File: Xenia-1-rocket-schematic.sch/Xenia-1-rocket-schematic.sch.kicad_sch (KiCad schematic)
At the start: 33 parts, among them M1 Stepper_Motor_bipolar, U3 A1115, U6 BME280, U7 Black_Box

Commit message: Schematic updated
Added a several new labels on the wiring diagram and made a section for the recovery altimeters, also made the e-matches necessary to light the black powder. Added recurring labels to wires on the right side and marked many ports with no X's to mean that they will not be connected to anything during wiring.
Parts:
- added U? (x8): E-Match, symbol Rocketry_project:E-Match
- added U? (x2): Raven4, symbol Rocketry_project:Raven4
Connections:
- net SDA is gone; now on net I2C Data: A?.3 (GPIO2/SDA), U?. (VDD), U?. (V_in), U?.~ (V_in), U?.~ (V_in)
- net +9V: now also U?.~ (V_in), U?.~ (V_in)
- net GND: now also A?.7 (GPIO4/GPCKL0), U?. (PCM_DOUT), U?. (Input), U?. (Input), U?. (Input), U?. (Input), U?. (Input), U?. (Input), U?. (Input), U?. (Input), U?.~ (V_in), U?.~ (V_in)
- net I2C Data: now reaches U?.~ (V_in)
- net APO: now reaches U?.~ (V_in)
- net APO: now also U?.~ (V_in), U?. (Input), U?. (Input), U?. (Input), U?. (Input), U?. (Input), U?. (Input), U?. (Input), U?. (Input)
- removed net GPIO4/Sleep: A?.7 (GPIO4/GPCKL0), U?. (PCM_DOUT), U?. (VMOT)
- removed net SCL: A?.5 (GPIO3/SCL), U?. (VDD), U?. (V_in), U?.~ (V_in), U?.~ (V_in)
- new net E-Match: U?.~ (V_in), U?.~ (V_in)
- new net I2C Clock: A?.5 (GPIO3/SCL), U?. (VDD), U?. (V_in), U?.~ (V_in), U?.~ (V_in)
- no-connect marks 30 -> 74
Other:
- note added: "Recovery Altimeters"

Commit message: Updated Schematic
Added a second sheet, and made a new version of the schematic that is a lot more organized
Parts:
- removed U? (x4): E-Match, symbol Rocketry_project:E-Match
- removed U? (x2): Transmitter, symbol Rocketry_project:Transmitter
- removed U?: Buzzer, symbol Rocketry_project:Buzzer
- added A?: rPi0w2, ADA3708_RPI-ZERO, symbol ADA3708:rPi0w2
- added BT? (x2): Battery_Cell, symbol Device:Battery_Cell
- added C?: CAP, symbol pspice:CAP
- added M?: Stepper_Motor_bipolar, symbol Motor:Stepper_Motor_bipolar
- added RV?: R_Potentiometer, symbol Device:R_Potentiometer
- added U1, U11, U12, U2, U? (x4): E-Match, symbol Rocketry_project:E-Match
- added U10, U31, U?: Transmitter, symbol Rocketry_project:Transmitter
- added U9, U?: Buzzer, symbol Rocketry_project:Buzzer
- added U?: Strain Gauge PCB, symbol Rocketry_project:Strain Gauge PCB
- added U? (x2): Raven4, symbol Rocketry_project:Raven4
- added U?: Camera, symbol Rocketry_project:Camera
- added U?: LSM9DS1, symbol Rocketry_project:LSM9DS1
- added U?: ADXL375, symbol Rocketry_project:ADXL375
- added U?: A1115, symbol Rocketry_project:A1115
- added U?: DRV8825, symbol Rocketry_project:DRV8825
- added U?: Black_Box, symbol Rocketry_project:Black_Box
- added U?: BME280, symbol Rocketry_project:BME280
- gave numbers to parts that had none: 31
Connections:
- net +3V8: now also U10. (TTL-DOUT)
- net 3V3: now also A?.1 (3V3[1]), U?. (V_in), U?.~ (V_in), U?.~ (V_in)
- net 5V: now also A?.2 (5V[1]), RV?.1, U?. (PCM_DOUT), U?. (VDD), U?. (VMOT)
- net APO: now also U1. (Input), U11. (Input), U2. (Input), U?. (Input), U?. (Input), U?. (Input), U?. (Input), U?.~ (V_in), U?.~ (V_in)
- net DIR: now also A?.26 (~{CE1/}GPIO7), U?. (PWR), U?. (VMOT)
- net Enable: now also A?.12 (GPIO18), U?. (VMOT)
- net GND: now also A?.9 (GND[1]), RV?.3, U1. (Input), U10. (TTL-DOUT), U11. (Input), U12. (Input), U2. (Input), U31. (TTL-DOUT), U9. (PWR), U?. (Input), U?. (Input), U?. (Input), U?. (Input), U?. (PCM_DOUT), U?. (PWR), U?. (TTL-DOUT), U?. (VDD), U?. (VMOT), U?. (V_in), U?.~ (V_in), U?.~ (V_in)
- net GPIO14: now also U10. (TTL-DOUT)
- net GPIO15: now also U10. (TTL-DOUT)
- net GPIO7: now also U9. (PWR)
- net I2C Clock: now also A?.5 (GPIO3/SCL), U?. (VDD), U?. (V_in), U?.~ (V_in), U?.~ (V_in)
- net I2C Data: now also A?.3 (GPIO2/SDA), U?. (VDD), U?. (V_in), U?.~ (V_in), U?.~ (V_in)
- net Step: now also A?.24 (~{CE0}/GPIO8), U?. (VMOT)
- net TTL-DIN: now also A?.8 (TXD0/GPIO14), U?. (TTL-DOUT)
- net TTL-DOUT: now also A?.10 (RXD0/GPIO15), U?. (TTL-DOUT)
- net at A2.10 (RXD0/GPIO15): now also U31. (TTL-DOUT)
- net at A2.8 (TXD0/GPIO14): now also U31. (TTL-DOUT)
- new net: A?. (Camera), U?.~ (Port)
- new net: A?.38 (GPIO20), U?. (PCM_DOUT)
- new net: A?.40 (GPIO21), U?. (PCM_DOUT)
- new net: A?.7 (GPIO4/GPCKL0), U?. (VMOT)
- new net: RV?.2, U?. (VDD)
- new net: BT?.1 (+), U?.~ (V_in) (x2)
- new net: BT?.2 (-), U?.~ (V_in) (x2)
- new net: M?.1, U?. (VMOT)
- new net: M?.2 (-), U?. (VMOT)
- new net: M?.3, U?. (VMOT)
- new net: M?.4, U?. (VMOT)
- new net: C?.1, U?. (VMOT)
- new net: C?.2, U?. (VMOT)
- no-connect marks 74 -> 73
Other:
- added sheet Sample wiring (untitled.kicad_sch)

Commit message: Updated Schematic
Made a couple adjustments to the schematic with the size of things and put a couple labels up
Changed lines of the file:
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@@
     (pin "1")
   )
-  (sheet (at 594.36 73.66) (size 748.03 304.8) (fields_autoplaced)
+  (sheet (at 594.36 73.66) (size 643.89 304.8) (fields_autoplaced)
     (stroke (width 0.1524) (type solid) (color 0 0 0 0))
     (fill (color 0 0 0 0.0000))

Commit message: Updated schematic
Added some labels to the second version of the wired schematic about what sides of the avionics bay things went to.
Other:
- note added: "Bottom of Avionics Bay"
- note added: "Top of Avionics Bay"
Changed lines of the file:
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@@
     (effects (font (size 3 3)) (justify left bottom))
+  )
+  (text "Side A" (at 1112.52 86.36 0)
+    (effects (font (size 2 2)) (justify left bottom))
   )
   (text "Side D" (at 524.51 209.55 0)
     (effects (font (size 3 3)) (justify left bottom))
+  )
+  (text "Top of Avionics Bay" (at 1167.13 83.82 0)
+    (effects (font (size 2 2)) (justify left bottom))
+  )
+  (text "Side B" (at 1112.52 144.78 0)
+    (effects (font (size 2 2)) (justify left bottom))
   )
   (text "Side A" (at 543.56 294.64 0)
@@
   (text "Inputs" (at 161.29 58.42 0)
     (effects (font (size 4 4)) (justify left bottom))
+  )
+  (text "Side C" (at 1109.98 231.14 0)
+    (effects (font (size 2 2)) (justify left bottom))
   )
   (text "Recovery Altimeters" (at 54.61 242.57 0)
@@
     (effects (font (size 1.27 1.27)) (justify left bottom))
   )
+  (text "Side D" (at 1111.25 293.37 0)
+    (effects (font (size 2 2)) (justify left bottom))
+  )
   (text "Analog to Digital Convertor" (at 240.03 143.51 0)
     (effects (font (size 1.27 1.27)) (justify left bottom))
   )
+  (text "Bottom of Avionics Bay" (at 645.16 102.87 0)
+    (effects (font (size 2 2)) (justify left bottom))
+  )
   (label "PCM_DOUT" (at 77.47 180.34 0)

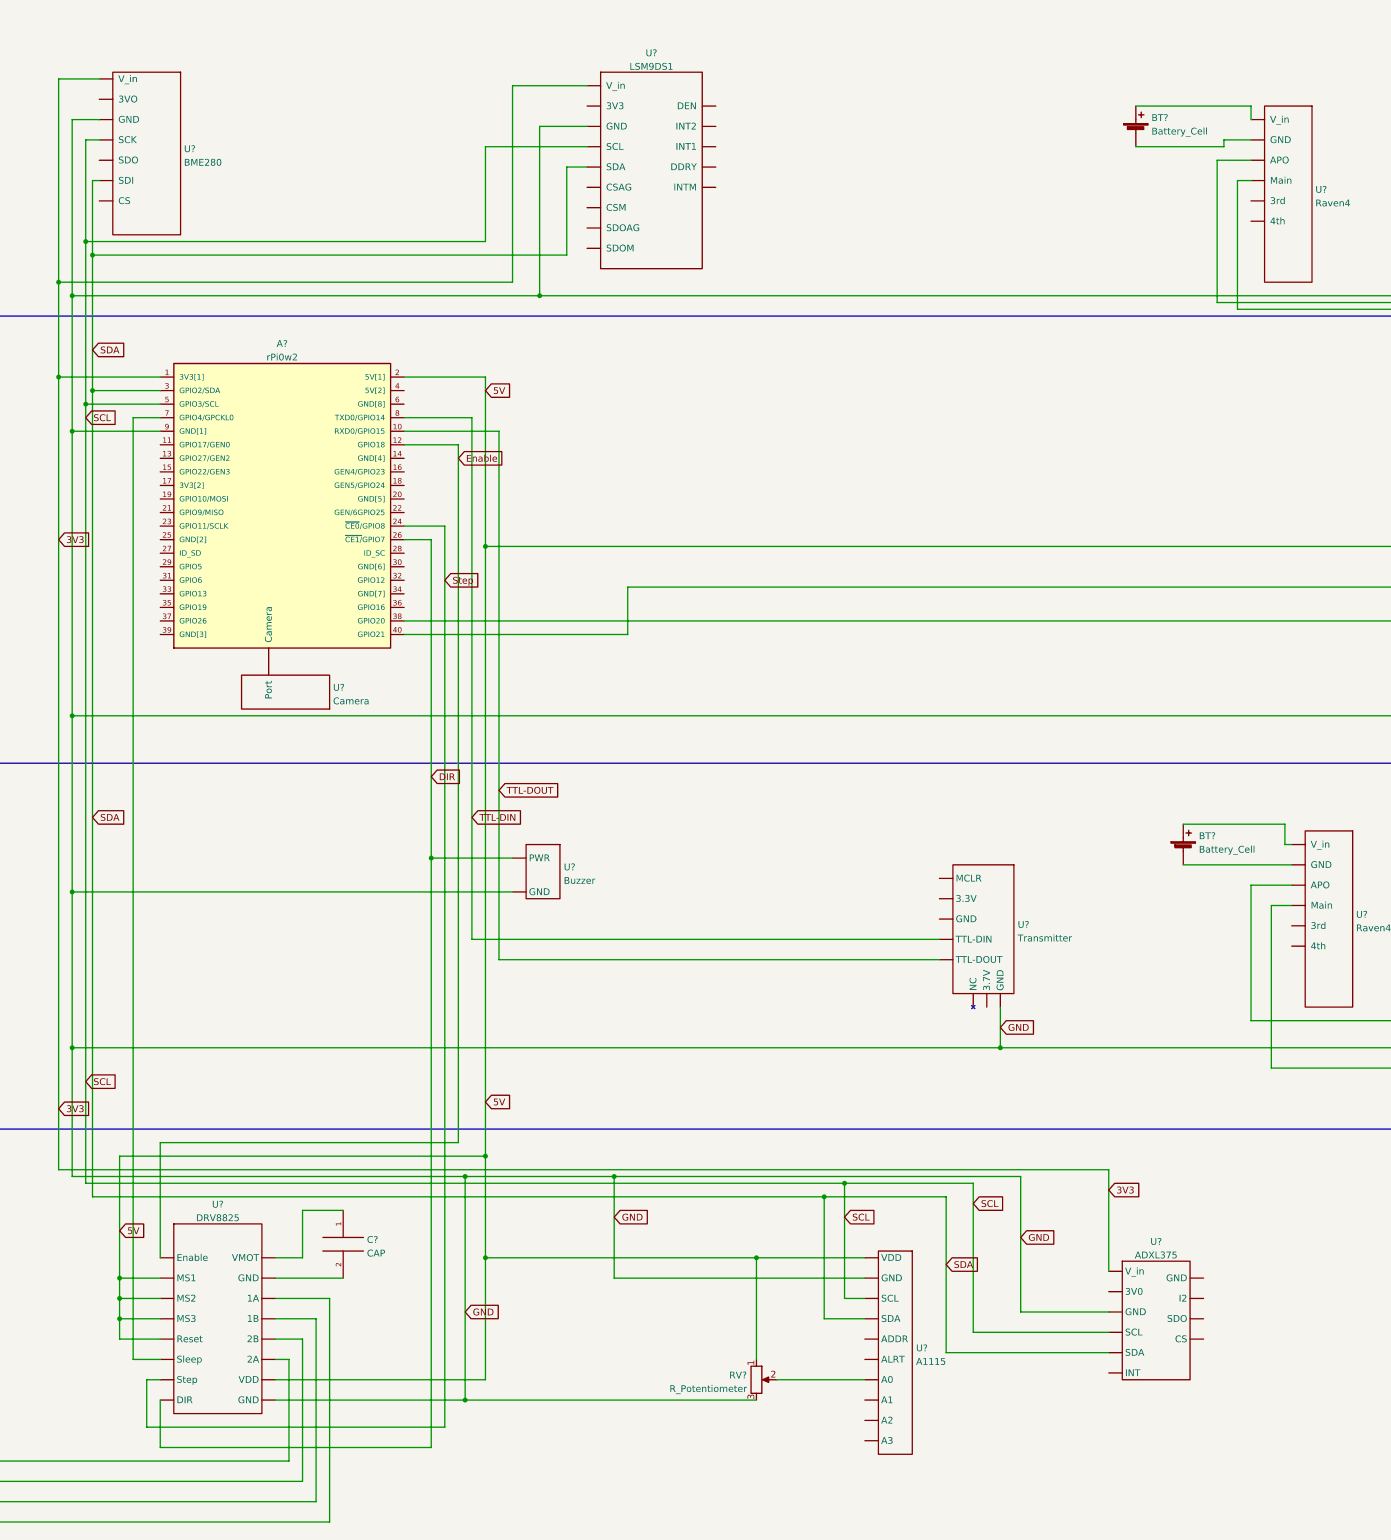
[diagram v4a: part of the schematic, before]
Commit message: Updated schematic
Marked many ports with no connect
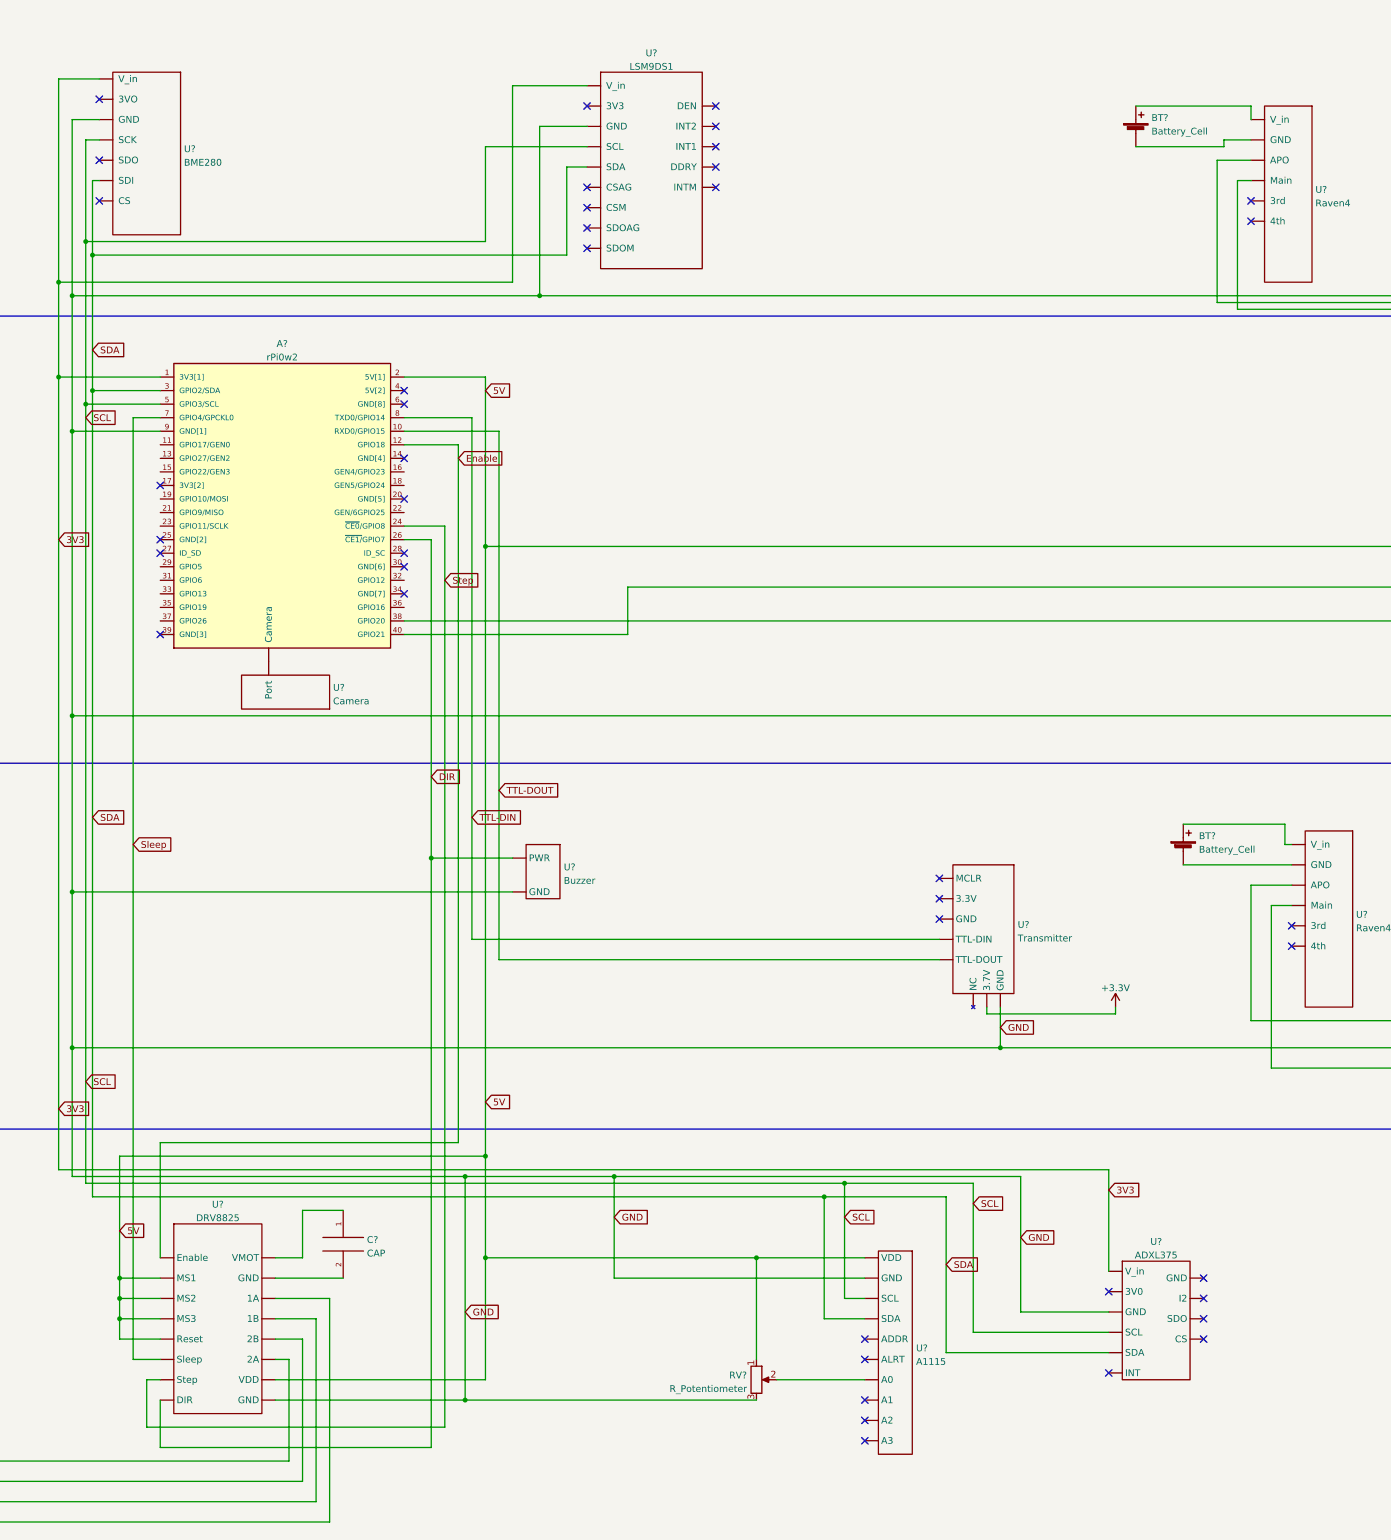
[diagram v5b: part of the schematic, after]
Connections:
- net +3V3: now also U?. (TTL-DOUT)
- net Sleep: now also A?.7 (GPIO4/GPCKL0), U?. (VMOT)
- no-connect marks 73 -> 115
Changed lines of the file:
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@@
   (no_connect (at 201.93 170.18))
   (no_connect (at 201.93 173.99))
+  (no_connect (at 932.18 111.76))
+  (no_connect (at 932.18 107.95))
+  (no_connect (at 932.18 104.14))
+  (no_connect (at 932.18 100.33))
+  (no_connect (at 932.18 96.52))
+  (no_connect (at 908.05 96.52))
+  (no_connect (at 908.05 111.76))
+  (no_connect (at 908.05 115.57))
+  (no_connect (at 908.05 119.38))
+  (no_connect (at 908.05 123.19))
+  (no_connect (at 816.61 114.3))
+  (no_connect (at 816.61 106.68))
+  (no_connect (at 816.61 95.25))
   (no_connect (at 146.05 158.75))
   (no_connect (at 146.05 143.51))
@@
   (no_connect (at 502.92 157.48))
   (no_connect (at 502.92 161.29))
+  (no_connect (at 873.76 187.96))
   (no_connect (at 100.33 62.23))
   (no_connect (at 100.33 58.42))
@@
   (no_connect (at 495.3 208.28))
   (no_connect (at 495.3 212.09))
+  (no_connect (at 873.76 149.86))
+  (no_connect (at 873.76 152.4))
+  (no_connect (at 873.76 162.56))
+  (no_connect (at 828.04 180.34))
+  (no_connect (at 828.04 177.8))
+  (no_connect (at 828.04 167.64))
+  (no_connect (at 873.76 170.18))
+  (no_connect (at 828.04 195.58))
+  (no_connect (at 873.76 182.88))
+  (no_connect (at 873.76 180.34))
   (no_connect (at 227.33 146.05))
   (no_connect (at 227.33 149.86))
@@
   (no_connect (at 227.33 196.85))
   (no_connect (at 227.33 177.8))
+  (no_connect (at 1032.51 114.3))
+  (no_connect (at 1032.51 118.11))
+  (no_connect (at 1040.13 250.19))
+  (no_connect (at 1040.13 254))
+  (no_connect (at 960.12 331.47))
+  (no_connect (at 960.12 339.09))
+  (no_connect (at 960.12 342.9))
+  (no_connect (at 960.12 327.66))
+  (no_connect (at 974.09 248.92))
+  (no_connect (at 974.09 245.11))
+  (no_connect (at 974.09 241.3))
+  (no_connect (at 960.12 346.71))
+  (no_connect (at 1005.84 334.01))
+  (no_connect (at 1005.84 318.77))
+  (no_connect (at 1023.62 316.23))
+  (no_connect (at 1023.62 320.04))
+  (no_connect (at 1023.62 323.85))
+  (no_connect (at 1023.62 327.66))
   (no_connect (at 77.47 165.1))
   (no_connect (at 77.47 167.64))
@@
     (stroke (width 0) (type default) (color 0 0 0 0))
   )
+  (wire (pts (xy 982.98 266.7) (xy 1007.11 266.7))
+    (stroke (width 0) (type default) (color 0 0 0 0))
+  )
   (wire (pts (xy 1158.24 140.97) (xy 1158.24 134.62))
     (stroke (width 0) (type default) (color 0 0 0 0))
@@
     (stroke (width 0) (type default) (color 0 0 0 0))
   )
+  (wire (pts (xy 982.98 265.43) (xy 982.98 266.7))
+    (stroke (width 0) (type default) (color 0 0 0 0))
+  )
   (wire (pts (xy 655.32 182.88) (xy 655.32 354.33))
     (stroke (width 0) (type default) (color 0 0 0 0))
@@
     (stroke (width 0) (type default) (color 0 0 0 0))
   )
+  (wire (pts (xy 1007.11 266.7) (xy 1007.11 265.43))
+    (stroke (width 0) (type default) (color 0 0 0 0))
+  )
   (wire (pts (xy 317.5 201.93) (xy 477.52 201.93))
     (stroke (width 0) (type default) (color 0 0 0 0))
@@
     )
   )
+  (global_label "Sleep" (shape input) (at 822.96 234.95 0) (fields_autoplaced)
+    (effects (font (size 1.27 1.27)) (justify left))
+    (property "Intersheet References" "${INTERSHEET_REFS}" (id 0) (at 830.4852 234.8706 0)
+      (effects (font (size 1.27 1.27)) (justify left) hide)
+    )
+  )
   (global_label "Main" (shape input) (at 513.08 62.23 0) (fields_autoplaced)
     (effects (font (size 1.27 1.27)) (justify left))
@@
     (pin "~")
   )
+  (symbol (lib_id "power:+3.3V") (at 1007.11 265.43 0) (unit 1)
+    (in_bom yes) (on_board yes) (fields_autoplaced)
+    (property "Reference" "#PWR?" (id 0) (at 1007.11 269.24 0)
+      (effects (font (size 1.27 1.27)) hide)
+    )
+    (property "Value" "+3.3V" (id 1) (at 1007.11 261.8542 0))
+    (property "Footprint" "" (id 2) (at 1007.11 265.43 0)
+      (effects (font (size 1.27 1.27)) hide)
+    )
+    (property "Datasheet" "" (id 3) (at 1007.11 265.43 0)
+      (effects (font (size 1.27 1.27)) hide)
+    )
+    (pin "1")
+  )
   (symbol (lib_id "Rocketry_project:DRV8825") (at 58.42 26.67 0) (unit 1)
     (in_bom yes) (on_board yes) (fields_autoplaced)
@@
       (reference "#PWR0102") (unit 1) (value "GND") (footprint "")
     )
+    (path "/49618dd1-0fe3-4495-8b48-479f9a6bad7d"
+      (reference "#PWR?") (unit 1) (value "+3.3V") (footprint "")
+    )
     (path "/ec5b882e-34a7-4655-9a50-380b50425bbd"
